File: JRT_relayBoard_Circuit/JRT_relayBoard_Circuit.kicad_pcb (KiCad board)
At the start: 2 copper layers, 3 parts, among them J1 Conn_ESP32_Left, J2 Conn_ESP32_Right, J3 37212-62M3-003PL

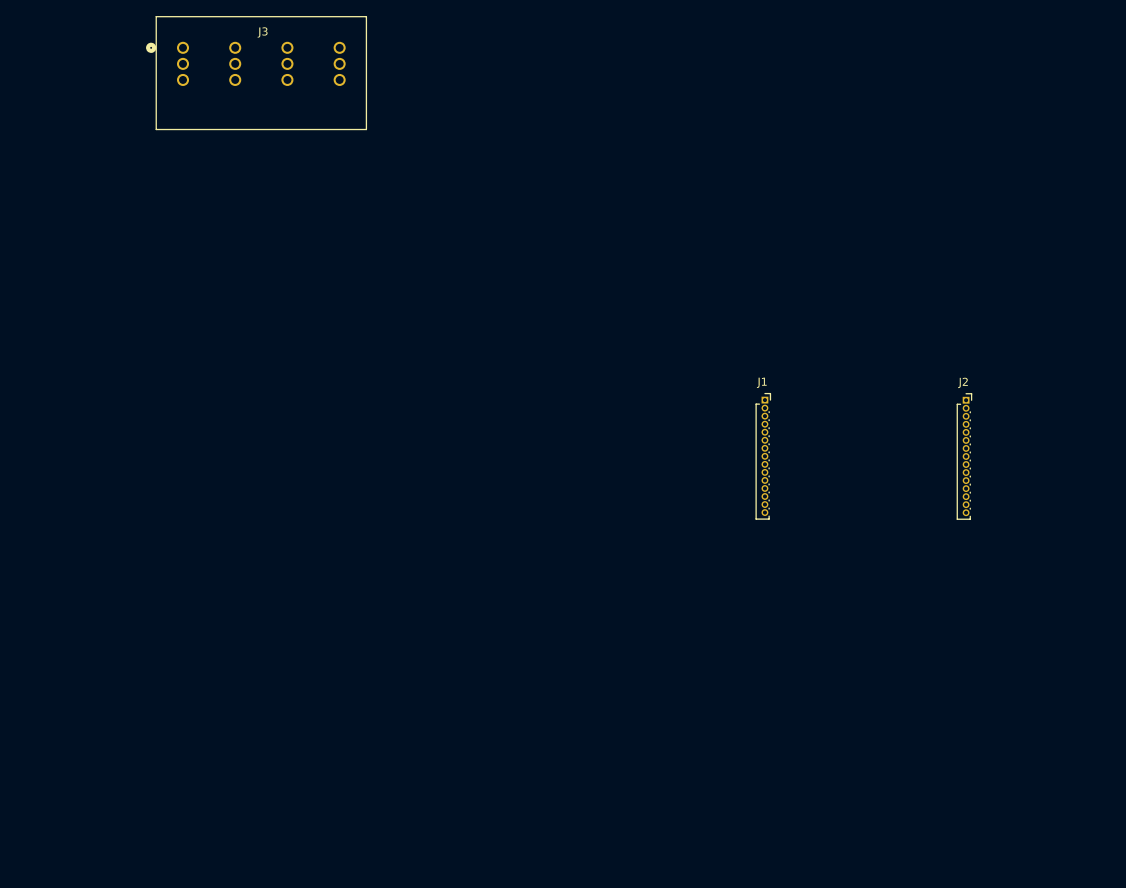
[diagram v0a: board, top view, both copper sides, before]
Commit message: コネクタの配置をした
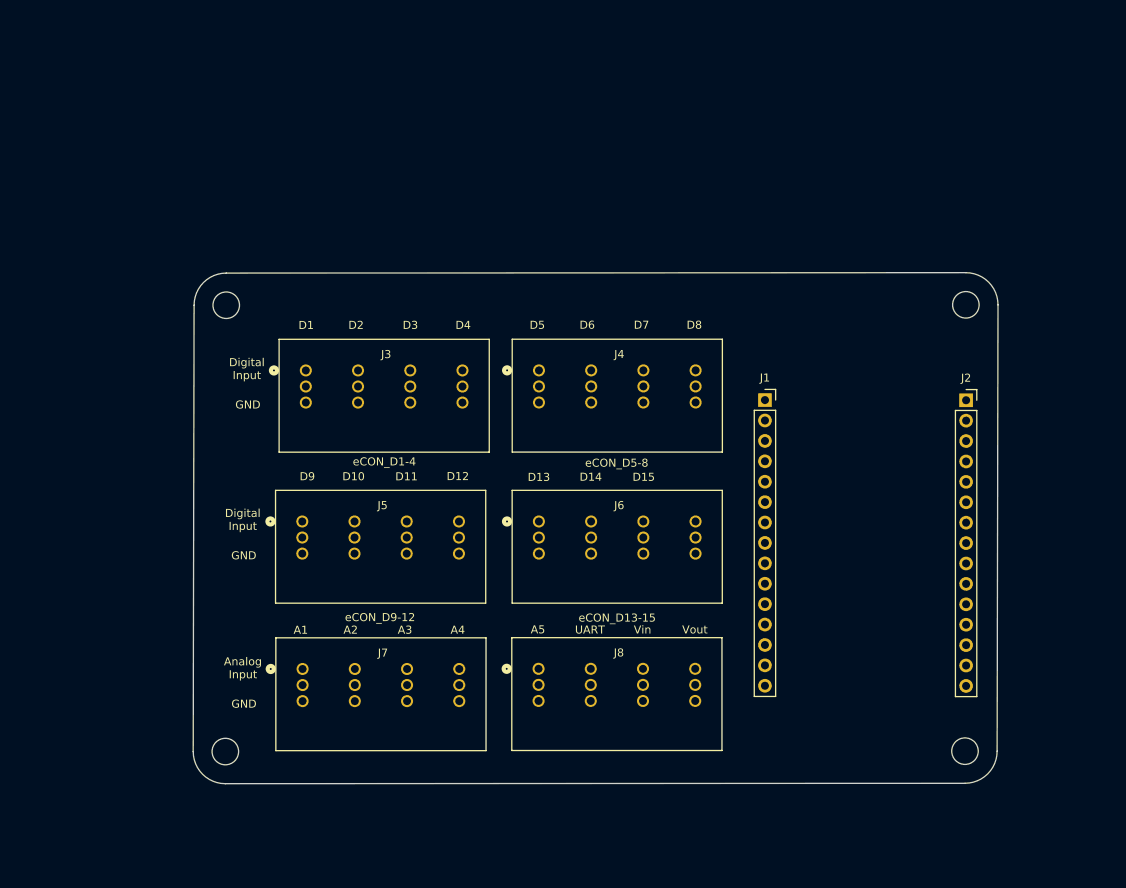
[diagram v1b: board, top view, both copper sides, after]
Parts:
- added J4: eCON_D5-8, eCon:CONN_37212-62M3-003PL_3MM, F.Cu at (129.0, 94.2)
- added J5: eCON_D9-12, eCon:CONN_37212-62M3-003PL_3MM, F.Cu at (99.5, 113.0)
- added J6: eCON_D13-15, eCon:CONN_37212-62M3-003PL_3MM, F.Cu at (129.0, 113.0)
- added J7: eCON_A1-4, eCon:CONN_37212-62M3-003PL_3MM, F.Cu at (99.6, 131.4)
- added J8: eCON_A5_UART_Vin_Vout, eCon:CONN_37212-62M3-003PL_3MM, F.Cu at (128.9, 131.4)
- J1, J2: footprint Connector_PinSocket_1.00mm:PinSocket_1x15_P1.00mm_Vertical -> Connector_PinSocket_2.54mm:PinSocket_1x15_P2.54mm_Vertical
- J3: value 37212-62M3-003PL -> eCON_D1-4
- moved J3 43.0 mm to (100.0, 94.2)
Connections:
- J3 pad 1: unconnected-(J3-Pad1) -> D1
- J3 pad 10: unconnected-(J3-Pad10) -> D4
- J3 pad 12: unconnected-(J3-Pad12) -> GND
- J3 pad 3: unconnected-(J3-Pad3) -> GND
- J3 pad 4: unconnected-(J3-Pad4) -> D2
- J3 pad 6: unconnected-(J3-Pad6) -> GND
- J3 pad 7: unconnected-(J3-Pad7) -> D3
- J3 pad 9: unconnected-(J3-Pad9) -> GND
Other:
- board outline added: 100.2 x 63.6 mm
- board text added: "A1"
- board text added: "A2"
- board text added: "A3"
- board text added: "A4"
- board text added: "A5"
- board text added: "Analog Input"
- board text added: "D1"
- board text added: "D10"
- board text added: "D11"
- board text added: "D12"
- board text added: "D13"
- board text added: "D14"
- board text added: "D15"
- board text added: "D2"
- board text added: "D3"
- board text added: "D4"
- board text added: "D5"
- board text added: "D6"
- board text added: "D7"
- board text added: "D8"
- board text added: "D9"
- board text added: "Digital Input"
- board text added: "GND"
- board text added: "UART"
- board text added: "Vin"
- board text added: "Vout"

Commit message: 配線を行った
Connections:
- J8 pad 4: UART-TX -> UART-RX
- J8 pad 5: UART-RX -> UART-TX
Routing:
- net +3.3V: track 0.00 -> 107.2 mm
- net A1: track 0.00 -> 88.0 mm
- net +9V: track 0.00 -> 87.9 mm
- net D9: track 0.00 -> 86.8 mm
- net A2: track 0.00 -> 79.4 mm
- net D10: track 0.00 -> 79.2 mm
- net GND1: track 0.00 -> 78.3 mm, vias 0 -> 2
- net A3: track 0.00 -> 72.4 mm
- net D11: track 0.00 -> 71.7 mm
- net D13: track 0.00 -> 71.6 mm, vias 0 -> 2
- net A4: track 0.00 -> 65.8 mm
- net D3: track 0.00 -> 65.7 mm, vias 0 -> 1
- net D12: track 0.00 -> 64.2 mm
- net D1: track 0.00 -> 62.2 mm
- net A5: track 0.00 -> 58.7 mm
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- added copper zone on B.Cu, net GND
- added copper zone on F.Cu, net GND
